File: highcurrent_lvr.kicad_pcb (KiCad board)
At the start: 2 copper layers, 58.4 x 51.4 mm, 22 parts, among them J1 Conn_01x02_Female, J2 Conn_01x02_Female, Q1 Q_NMOS_DGS, Q2 Q_NMOS_DGS, U1 LTC4365DDB, U2 MIC29303WU

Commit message: fixed pcb layout
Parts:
- removed D1, D2, D3: LED, LED_SMD:LED_0805_2012Metric_Pad1.15x1.40mm_HandSolder
- removed HS1: Heatsink, Heatsink:547-95AB
- removed J1, J2: Conn_01x02_Female, TerminalBlock_Phoenix:TerminalBlock_Phoenix_MKDS-1,5-2_1x02_P5.00mm_Horizontal
- removed R7, R8, R9: 1k, Resistor_SMD:R_0805_2012Metric_Pad1.20x1.40mm_HandSolder
- added POWER_IN: Conn_01x02_Female, TerminalBlock_Phoenix:TerminalBlock_Phoenix_MKDS-1,5-2_1x02_P5.00mm_Horizontal, F.Cu at (431.8, 186.7)
- added POWER_OUT: Conn_01x02_Female, TerminalBlock_Phoenix:TerminalBlock_Phoenix_MKDS-1,5-2_1x02_P5.00mm_Horizontal, F.Cu at (457.8, 186.7)
- R1, R2, R3, R4, R5: footprint Resistor_SMD:R_0805_2012Metric_Pad1.20x1.40mm_HandSolder -> Resistor_SMD:R_0805_2012Metric_Pad1.15x1.40mm_HandSolder
- moved Q1 296.5 mm to (459.1, 162.1), turned to 180 degrees
- moved R6 284.5 mm to (436.2, 159.4), turned to 180 degrees
- moved R5 284.5 mm to (438.1, 165.1), turned to 90 degrees
- moved U2 281.1 mm to (428.7, 167.5)
- moved Q2 280.6 mm to (459.2, 170.9), turned to 0 degrees
- moved C3 276.7 mm to (429.1, 160.0)
- moved R2 275.3 mm to (447.0, 163.6), turned to 180 degrees
- moved R3 275.3 mm to (447.0, 161.4)
- moved R1 274.8 mm to (447.0, 165.9), turned to 180 degrees
- moved U1 274.5 mm to (451.1, 162.7), turned to 0 degrees
- moved R4 273.8 mm to (450.5, 159.5)
- moved C2 273.8 mm to (429.1, 175.3), turned to 180 degrees
- moved C1 273.7 mm to (456.2, 176.0), turned to 0 degrees
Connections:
- net Net-(R1-Pad2) renamed /Cutoff/uv_sense
- net Net-(R2-Pad2) renamed /Cutoff/ov_sense
- U1 pad 7: /error -> (no net)
- U2 pad 1: /supp_error -> (no net)
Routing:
- net /reg_out: track 18.2 -> 51.7 mm, vias 0 -> 2
- net GND: track 3.90 -> 29.1 mm, vias 119 -> 162
- net Net-(Q1-Pad1): track 29.9 -> 19.4 mm, vias 0 -> 2
- net VCC: track 0.00 -> 9.43 mm
- net /error: track 8.45 -> 0.00 mm, vias 3 -> 0
- net /vout: track 23.1 -> 16.5 mm, vias 2 -> 0
- net /supp_error: track 5.65 -> 0.00 mm
- net Net-(R5-Pad2): track 12.2 -> 7.47 mm
- net Net-(D3-Pad2): track 4.66 -> 0.00 mm
- net Net-(D1-Pad2): track 4.34 -> 0.00 mm
- net /Cutoff/ov_sense: track 10.0 -> 6.29 mm, vias 2 -> 0
- net /Cutoff/uv_sense: track 9.93 -> 6.26 mm, vias 3 -> 0
- net Net-(D2-Pad2): track 2.16 -> 0.00 mm
- net Net-(R4-Pad1): track 6.50 -> 4.36 mm
- added copper zone on F.Cu, net /vout
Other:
- board size 58.4 x 51.4 mm -> 54.6 x 36.2 mm
- board text added: "+"
- board text added: "-"
- board text added: "1) 18V Input"
- board text added: "2) 2A Input"
- board text added: "3) Regulator Temp <100C"
- board text added: "CAUTION: HOT"
- board text added: "Design Ratings"

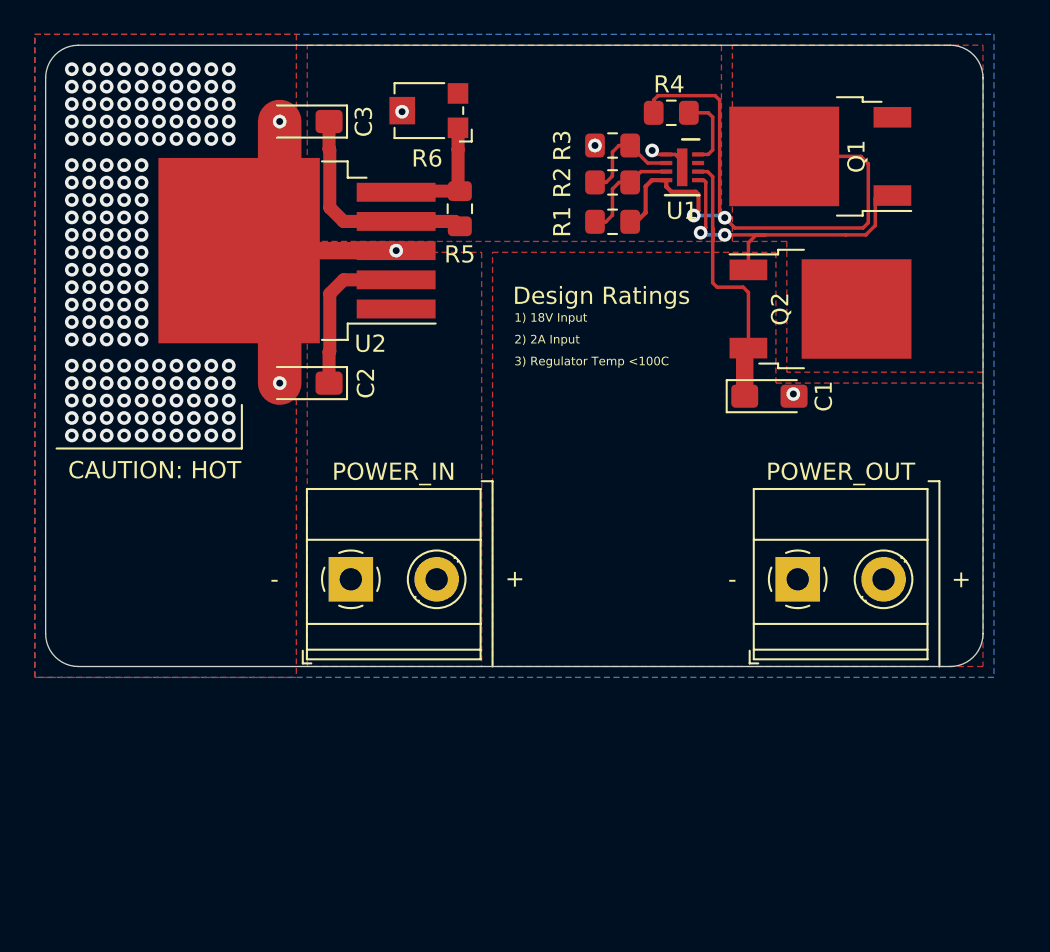
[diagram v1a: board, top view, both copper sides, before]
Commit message: added new heatsink alterantive
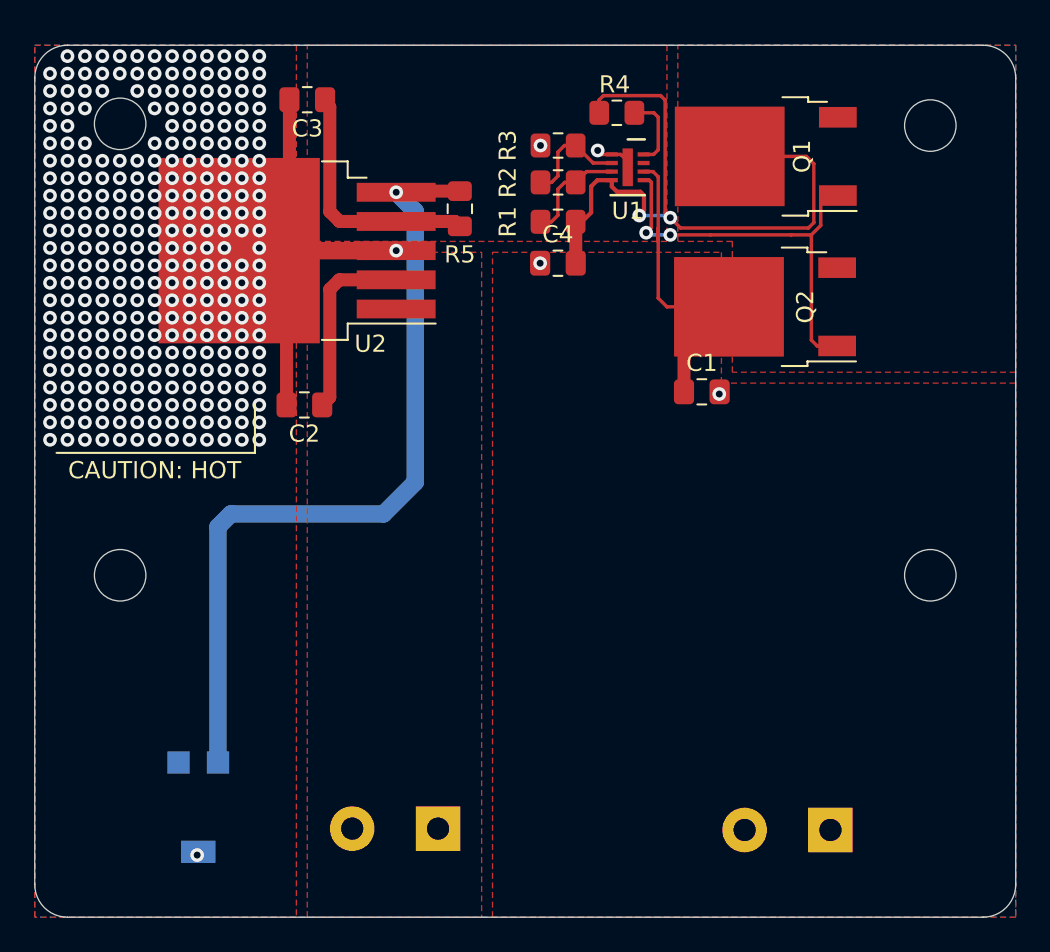
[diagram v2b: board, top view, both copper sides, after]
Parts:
- added C4: 4.7uF, Capacitor_SMD:C_0805_2012Metric_Pad1.18x1.45mm_HandSolder, F.Cu at (443.9, 168.3)
- added HS1: Heatsink, heatsink-lib:ATS-1139-C1-R0, B.Cu at (442.0, 173.4)
- C1, C2, C3: footprint Capacitor_Tantalum_SMD:CP_EIA-3216-12_Kemet-S_Pad1.58x1.35mm_HandSolder -> Capacitor_SMD:C_0805_2012Metric_Pad1.18x1.45mm_HandSolder
- POWER_IN1: renamed from POWER_IN; moved to B.Cu
- POWER_OUT1: renamed from POWER_OUT; moved to B.Cu
- R6: footprint Potentiometer_SMD:Potentiometer_Bourns_TC33X_Vertical -> Potentiometer_SMD:Potentiometer_Bourns_3224G_Horizontal; moved to B.Cu
- moved R6 42.7 mm to (422.9, 200.0), turned to 90 degrees
- moved POWER_IN1 15.4 mm to (436.9, 201.2), turned to 180 degrees
- moved POWER_OUT1 14.7 mm to (459.7, 201.3), turned to 180 degrees
- moved C1 3.95 mm to (452.2, 175.8)
- moved Q2 3.24 mm to (455.9, 170.8), turned to 180 degrees
- moved Q1 3.18 mm to (456.0, 162.1)
- moved R4 3.18 mm to (447.3, 159.5)
- moved U1 3.18 mm to (447.9, 162.7)
- moved R1 3.17 mm to (443.9, 165.9)
- moved R2 3.17 mm to (443.9, 163.6)
- moved R3 3.17 mm to (443.9, 161.4)
- moved C3 1.28 mm to (429.3, 158.8)
- moved C2 1.27 mm to (429.1, 176.5)
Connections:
- Q2 pad 2: Net-(Q1-Pad3) -> /vout
- Q2 pad 3: /vout -> Net-(Q1-Pad3)
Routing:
- net Net-(R5-Pad2): track 7.47 -> 47.3 mm, vias 0 -> 1
- net Net-(Q1-Pad1): track 19.4 -> 24.4 mm
- net /reg_out: track 51.7 -> 55.6 mm
- net GND: track 29.1 -> 32.3 mm, vias 162 -> 291
- net /vout: track 16.5 -> 19.2 mm
- net VCC: track 9.43 -> 11.2 mm
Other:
- board size 54.6 x 36.2 mm -> 57.2 x 50.8 mm
- board text removed: "1) 18V Input"
- board text removed: "2) 2A Input"
- board text removed: "3) Regulator Temp <100C"
- board text removed: "Design Ratings"

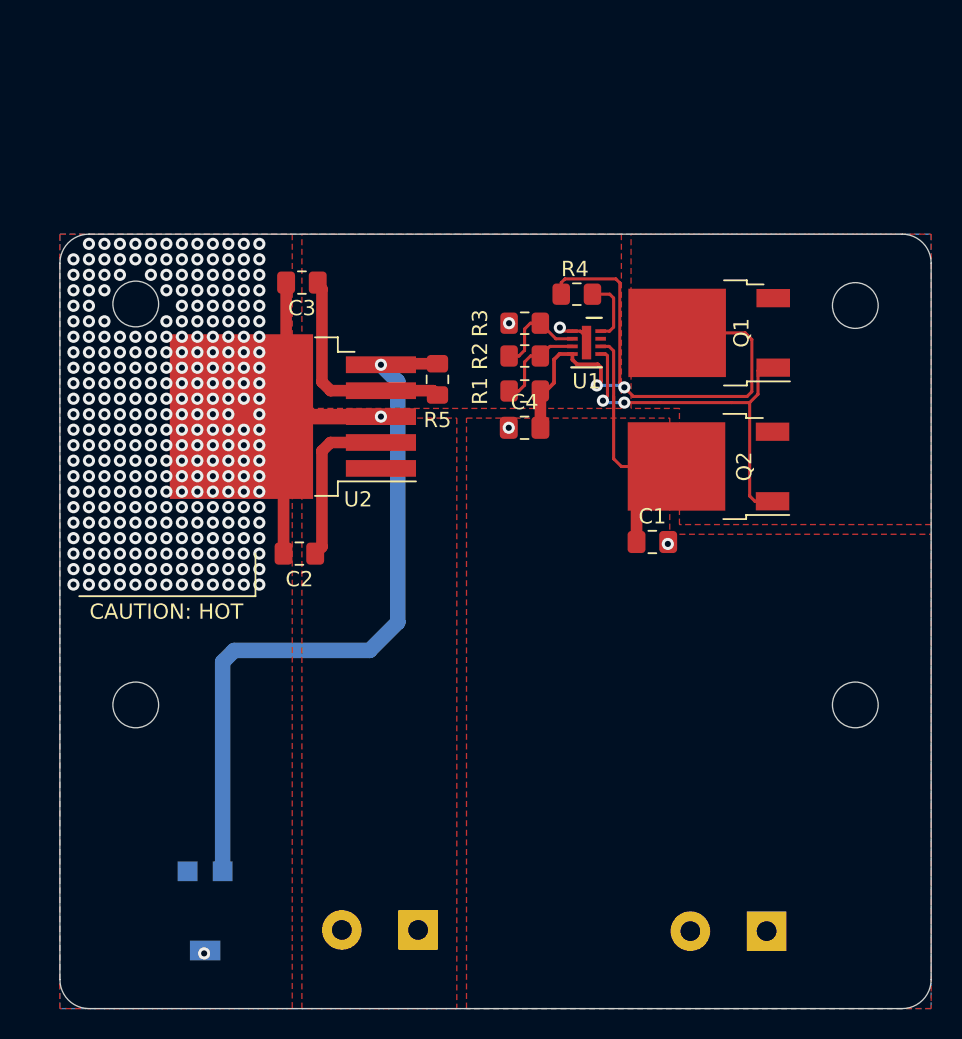
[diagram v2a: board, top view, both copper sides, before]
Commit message: changed layout for heat sink w/ issue #1
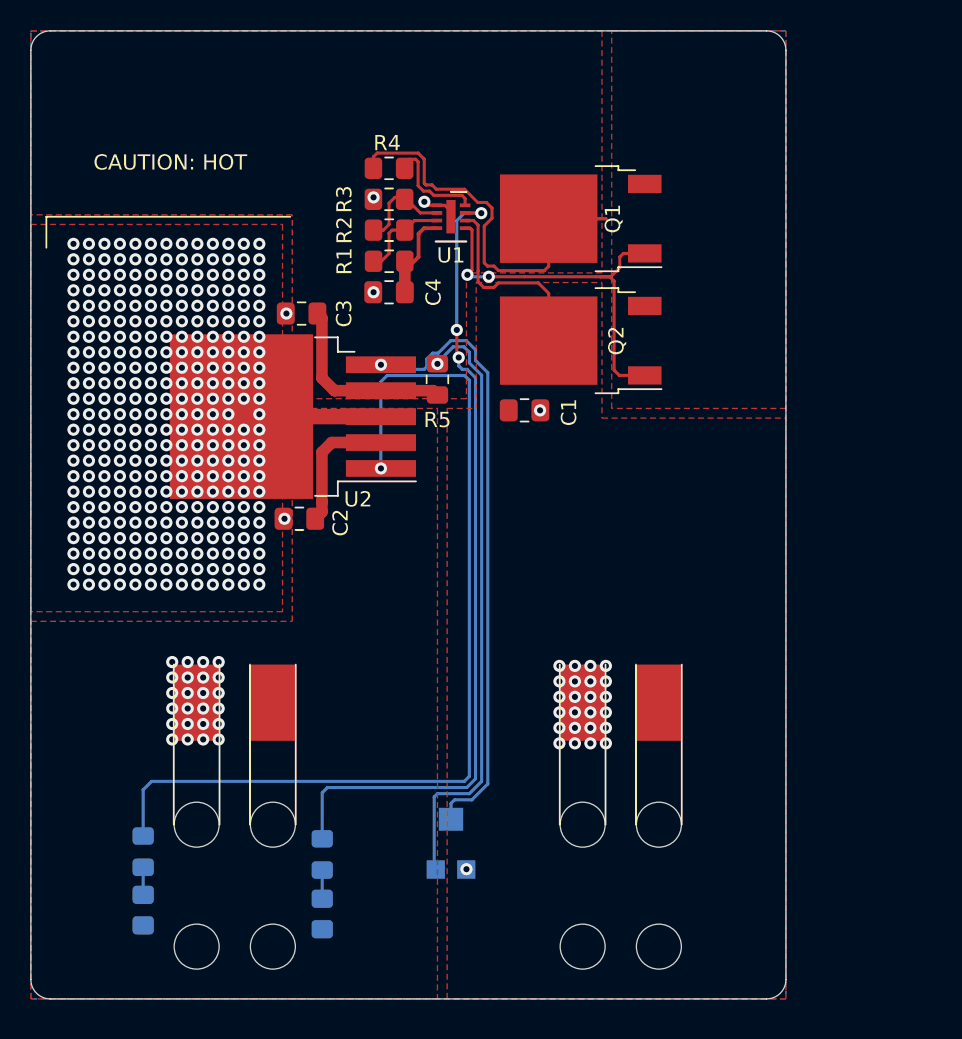
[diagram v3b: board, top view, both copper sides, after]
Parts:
- added D1: LED, LED_SMD:LED_0805_2012Metric_Pad1.15x1.40mm_HandSolder, B.Cu at (430.6, 196.3)
- added D2: LED, LED_SMD:LED_0805_2012Metric_Pad1.15x1.40mm_HandSolder, B.Cu at (418.8, 196.1)
- added R7: 1k8, Resistor_SMD:R_0805_2012Metric_Pad1.20x1.40mm_HandSolder, B.Cu at (430.6, 200.2)
- added RV1: R_POT, potentiometer-lib:TC33X-2-201G, B.Cu at (439.0, 195.5)
- HS1: footprint heatsink-lib:ATS-1139-C1-R0 -> heatsink-lib:Ohmite-BGAH450125E
- POWER_IN1, POWER_OUT1: footprint TerminalBlock_Phoenix:TerminalBlock_Phoenix_MKDS-1,5-2_1x02_P5.00mm_Horizontal -> wire-connector-lib:connector-wire-3cm2-2pin-smd; moved to F.Cu
- R6: value 0 - 200 -> 1k8; footprint Potentiometer_SMD:Potentiometer_Bourns_3224G_Horizontal -> Resistor_SMD:R_0805_2012Metric_Pad1.20x1.40mm_HandSolder
- moved R4 14.8 mm to (435.0, 151.3)
- moved POWER_IN1 13.9 mm to (424.9, 194.3), turned to 0 degrees
- moved C4 12.6 mm to (435.0, 159.4)
- moved R1 12.3 mm to (435.0, 157.4)
- moved R2 12.1 mm to (435.0, 155.3)
- moved U1 12.1 mm to (439.0, 154.4)
- moved R3 12.1 mm to (435.0, 153.3)
- moved C1 12.0 mm to (443.9, 167.1)
- moved POWER_OUT1 11.8 mm to (450.2, 194.3), turned to 0 degrees
- moved Q2 11.8 mm to (447.5, 162.6)
- moved Q1 11.3 mm to (447.5, 154.6)
- moved HS1 8.54 mm to (436.2, 167.0), turned to 0 degrees
- moved R6 4.06 mm to (418.8, 199.9), turned to 270 degrees
- moved C2 2.29 mm to (429.1, 174.2)
- moved C3 2.03 mm to (429.2, 160.8)
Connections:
- R6 pad 1: Net-(R5-Pad2) -> Net-(D2-Pad1)
- U1 pad 7: (no net) -> /error
- U2 pad 1: (no net) -> /supp_error
- U2 pad 5: Net-(R5-Pad2) -> Net-(RV1-Pad2)
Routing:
- net /supp_error: track 0.00 -> 62.6 mm, vias 0 -> 1
- net /error: track 0.00 -> 54.2 mm, vias 0 -> 3
- net Net-(RV1-Pad2): track 0.00 -> 40.5 mm, vias 0 -> 1
- net GND: track 32.3 -> 11.9 mm, vias 291 -> 353
- net /reg_out: track 55.6 -> 47.7 mm, vias 2 -> 0
- net Net-(R5-Pad2): track 47.3 -> 39.6 mm
- net /vout: track 19.2 -> 13.0 mm
- net Net-(Q1-Pad1): track 24.4 -> 27.2 mm
- net VCC: track 11.2 -> 8.68 mm
- net Net-(R4-Pad1): track 4.36 -> 6.80 mm
- net Net-(D1-Pad1): track 0.00 -> 1.88 mm
- net Net-(D2-Pad1): track 0.00 -> 1.81 mm
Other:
- board size 57.2 x 50.8 mm -> 49.5 x 63.5 mm
- board text added: "GND"
- board text added: "IN"
- board text added: "OUT"
- board text added: "OV_Err"
- board text added: "Reg_Err"
- board text removed: "+"
- board text removed: "-"

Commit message: added panelization
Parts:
- added H1: MountingHole, MountingHole:MountingHole_4mm, F.Cu at (134.6, 57.8)
- added H2: MountingHole, MountingHole:MountingHole_4mm, F.Cu at (163.8, 57.8)
- added H3: MountingHole, MountingHole:MountingHole_4mm, F.Cu at (134.6, 126.4)
- added H4: MountingHole, MountingHole:MountingHole_4mm, F.Cu at (163.8, 126.4)
- moved C1 298.5 mm to (156.8, 85.2)
- moved C2 298.5 mm to (142.1, 92.3)
- moved C3 298.5 mm to (142.2, 78.9)
- moved C4 298.5 mm to (148.0, 77.5)
- moved D1 298.5 mm to (143.6, 114.3)
- moved D2 298.5 mm to (131.8, 114.2)
- moved HS1 298.5 mm to (149.2, 85.1)
- moved POWER_IN1 298.5 mm to (137.8, 112.4)
- moved POWER_OUT1 298.5 mm to (163.2, 112.4)
- moved Q1 298.5 mm to (160.5, 72.6)
- moved Q2 298.5 mm to (160.5, 80.6)
- moved R1 298.5 mm to (148.0, 75.4)
- moved R2 298.5 mm to (148.0, 73.4)
- moved R3 298.5 mm to (148.0, 71.4)
- moved R4 298.5 mm to (148.0, 69.3)
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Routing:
- net /error: track 54.2 -> 54.9 mm
- net /supp_error: track 62.6 -> 63.3 mm
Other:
- board size 49.5 x 63.5 mm -> 49.5 x 76.2 mm
